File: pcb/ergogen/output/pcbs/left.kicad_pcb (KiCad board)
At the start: 2 copper layers, 135.6 x 74.7 mm, 62 parts

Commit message: Check the hotswap sockets on the PCB underside; move connectors clear of them
The socket footprints sit on the front layer, so the back-side checks skipped
them. Now the socket bodies are modeled and checked against nuts, connectors,
posts, poron, battery, screens, ball unit and switch cover (also at full PCB travel).

- Battery connectors (left/right) and the sensor connector J1 moved into free spots
- Tray rim trimmed under the outer-column sockets at the top-right corner

Co-Authored-By: Claude Opus 5.5 <noreply@anthropic.com>
Claude-Session: https://claude.ai/code/session_017zNm7dMSTHELcztuNr6aNy
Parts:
- moved BAT1 19.0 mm to (48.0, -29.0), turned to 0 degrees
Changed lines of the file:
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@@
       )
       (module "Connector_Molex:Molex_PicoBlade_53261-0271_1x02-1MP_P1.25mm_Horizontal" (layer B.Cu)
-      (at 29 -29 90)
-      (fp_text reference "BAT1" (at 0 4.4 90) (layer B.SilkS) hide (effects (font (size 1 1) (thickness 0.15)) (justify mirror)))
-      (fp_text value "Molex_PicoBlade_53261-0271_1x02-1MP_P1.25mm_Horizontal" (at 0 0 90) (layer B.Fab) hide (effects (font (size 0.8 0.8) (thickness 0.12)) (justify mirror)))
+      (at 48 -29 0)
+      (fp_text reference "BAT1" (at 0 4.4 0) (layer B.SilkS) hide (effects (font (size 1 1) (thickness 0.15)) (justify mirror)))
+      (fp_text value "Molex_PicoBlade_53261-0271_1x02-1MP_P1.25mm_Horizontal" (at 0 0 0) (layer B.Fab) hide (effects (font (size 0.8 0.8) (thickness 0.12)) (justify mirror)))
       (fp_line (start -2.235 1.71) (end -1.285 1.71) (layer B.SilkS) (width 0.12))
       (fp_line (start -2.235 1.26) (end -2.235 1.71) (layer B.SilkS) (width 0.12))
@@
       (fp_line (start 3.825 0.4) (end 3.825 -1.4) (layer B.Fab) (width 0.1))
       (fp_line (start 3.825 -1.4) (end 3.625 -1.6) (layer B.Fab) (width 0.1))
-      (pad "1" smd roundrect (at -0.625 2.4 90) (size 0.8 1.6) (roundrect_rratio 0.25) (layers B.Cu B.Mask B.Paste) (net 38 "GND"))
-      (pad "2" smd roundrect (at 0.625 2.4 90) (size 0.8 1.6) (roundrect_rratio 0.25) (layers B.Cu B.Mask B.Paste) (net 45 "BAT_P"))
-      (pad "MP" smd roundrect (at -3.175 -0.5 90) (size 2.1 3) (roundrect_rratio 0.119048) (layers B.Cu B.Mask B.Paste))
-      (pad "MP" smd roundrect (at 3.175 -0.5 90) (size 2.1 3) (roundrect_rratio 0.119048) (layers B.Cu B.Mask B.Paste))
+      (pad "1" smd roundrect (at -0.625 2.4 0) (size 0.8 1.6) (roundrect_rratio 0.25) (layers B.Cu B.Mask B.Paste) (net 38 "GND"))
+      (pad "2" smd roundrect (at 0.625 2.4 0) (size 0.8 1.6) (roundrect_rratio 0.25) (layers B.Cu B.Mask B.Paste) (net 45 "BAT_P"))
+      (pad "MP" smd roundrect (at -3.175 -0.5 0) (size 2.1 3) (roundrect_rratio 0.119048) (layers B.Cu B.Mask B.Paste))
+      (pad "MP" smd roundrect (at 3.175 -0.5 0) (size 2.1 3) (roundrect_rratio 0.119048) (layers B.Cu B.Mask B.Paste))
       (model "${KICAD10_3DMODEL_DIR}/Connector_Molex.3dshapes/Molex_PicoBlade_53261-0271_1x02-1MP_P1.25mm_Horizontal.step")
       )

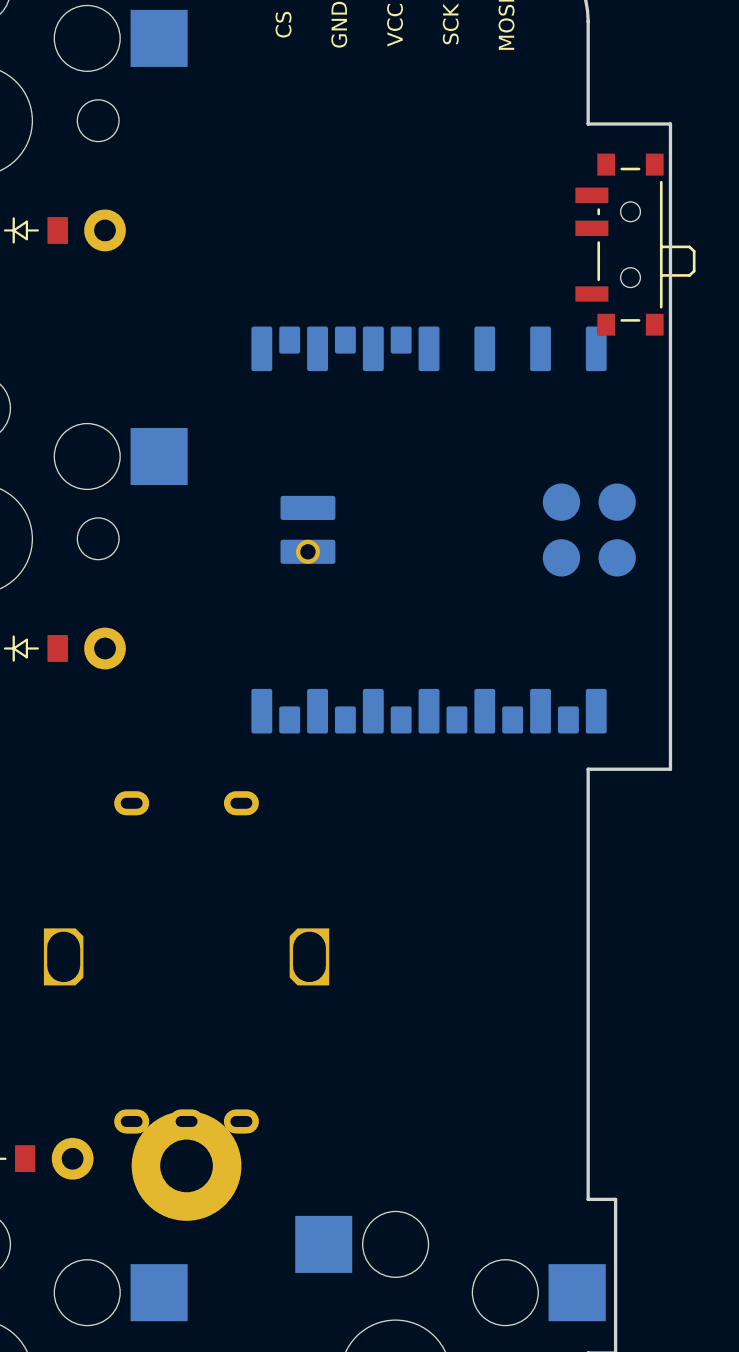
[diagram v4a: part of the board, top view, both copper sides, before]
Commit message: Ukishima: full PCB parts list and height stack; fix clashes it revealed
- check_pcb reads KiCad 8 footprints too (the encoder was skipped): the post
  under the encoder pins moved to a free spot under the encoder
- All back-side parts (XIAO, connectors, SOD-123 diodes, nuts, trimmed pins,
  sockets) are modeled with heights and checked at full PCB travel
- PCB raised 0.3mm so a thicker battery (+0.3) still clears the sockets
- Tray wall recessed under the XIAO end; power switch moved 1mm back so its
  cover clears the XIAO
- nice!view height from a standard 2.5mm pin header; switch cover heights follow the PCB
- docs: parts table (incl. no resistors needed) and height stack

Co-Authored-By: Claude Opus 5.5 <noreply@anthropic.com>
Claude-Session: https://claude.ai/code/session_017zNm7dMSTHELcztuNr6aNy
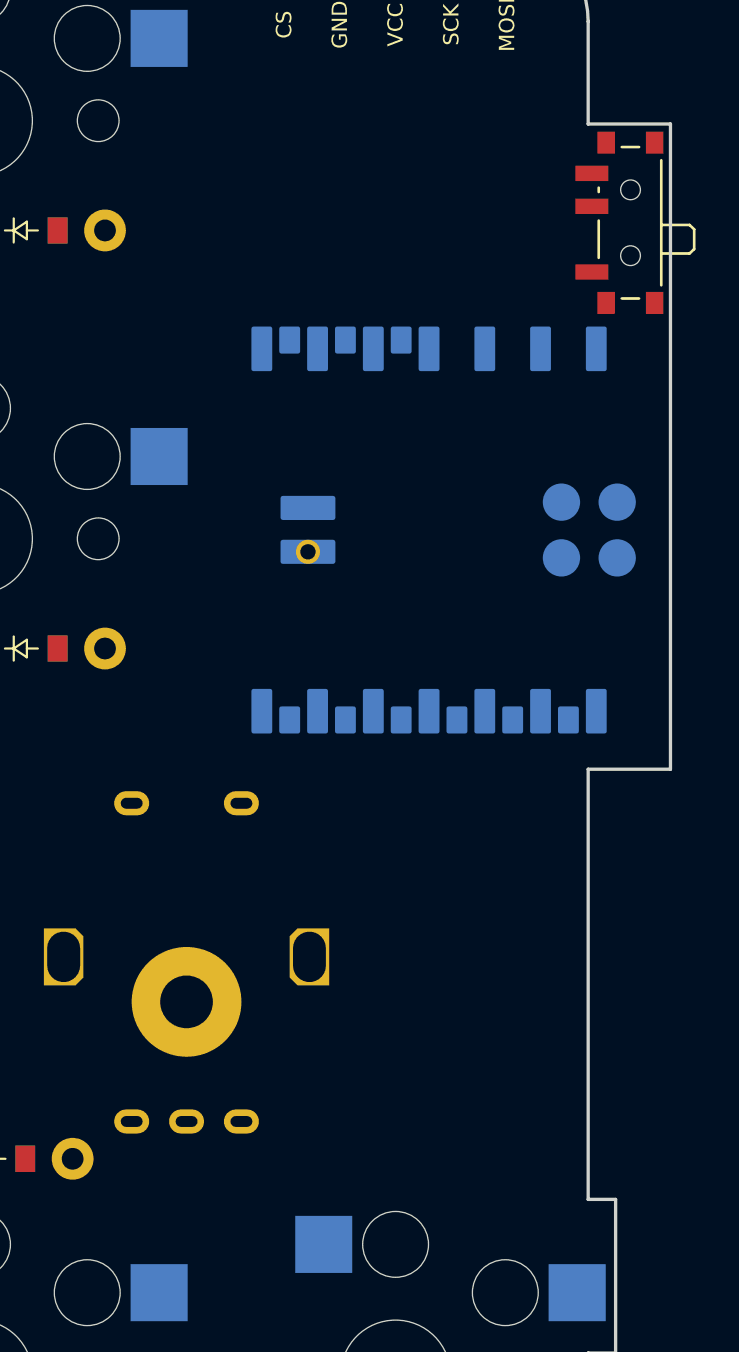
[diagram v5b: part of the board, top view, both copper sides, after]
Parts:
- moved H4 7.47 mm to (104.8, -17.0)
- moved PWR1 1.00 mm to (124.7, -52.5)
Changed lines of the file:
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@@
       )
       (module "Button_Switch_SMD:SW_SPDT_PCM12" (layer F.Cu)
-      (at 124.675 -51.5 90)
+      (at 124.675 -52.5 90)
       (fp_text reference "PWR1" (at 0 -3.2 90) (layer F.SilkS) hide (effects (font (size 1 1) (thickness 0.15)) ))
       (fp_text value "SW_SPDT_PCM12" (at 0 0 90) (layer F.Fab) hide (effects (font (size 0.8 0.8) (thickness 0.12)) ))
@@
       )
       (module "kataware:SMT_Nut_M2" (layer B.Cu)
-      (at 104.775 -9.525 0)
+      (at 104.775 -17 0)
       (fp_text reference "H4" (at 0 3.6 0) (layer B.SilkS) hide (effects (font (size 0.8 0.8) (thickness 0.12)) (justify mirror)))
       (fp_text value "SMT_Nut_M2" (at 0 0 0) (layer B.Fab) hide (effects (font (size 0.8 0.8) (thickness 0.12))))
